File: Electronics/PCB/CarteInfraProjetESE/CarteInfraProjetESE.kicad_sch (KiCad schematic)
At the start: 4 parts

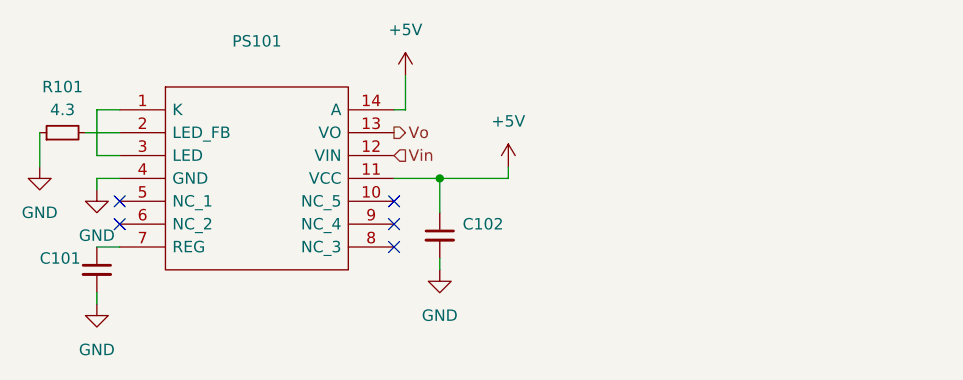
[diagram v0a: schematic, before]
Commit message: added test pin
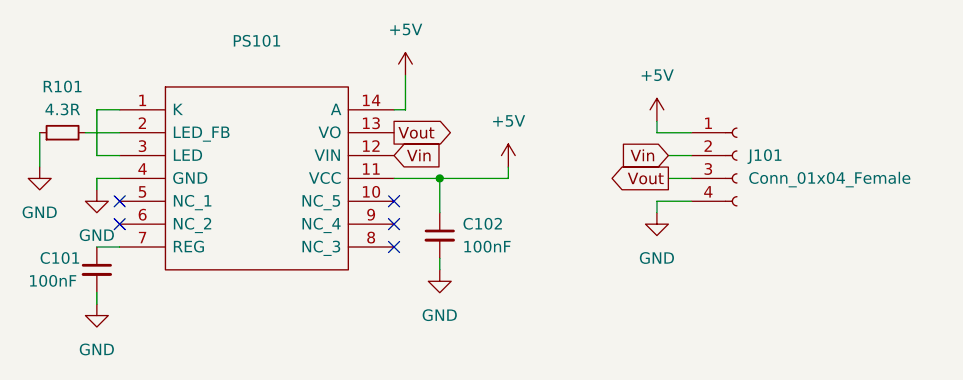
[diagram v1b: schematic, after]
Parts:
- added J101: Conn_01x04_Female, symbol Connector:Conn_01x04_Female
- C101, C102: value ~ -> 100nF
- R101: value 4.3 -> 4.3R
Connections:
- net +5V: now also J101.1 (Pin_1)
- net GND: now also J101.4 (Pin_4)
- net Vin: now also J101.2 (Pin_2)
- net Vo renamed Vout
- net Vout: now also J101.3 (Pin_3)
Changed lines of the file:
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@@
+    (stroke (width 0) (type default) (color 0 0 0 0))
+  )
+  (wire (pts (xy 191.77 74.93) (xy 194.31 74.93))
+    (stroke (width 0) (type default) (color 0 0 0 0))
+  )
+  (wire (pts (xy 190.5 71.12) (xy 190.5 72.39))
     (stroke (width 0) (type default) (color 0 0 0 0))
   )
@@
     (stroke (width 0) (type default) (color 0 0 0 0))
   )
+  (wire (pts (xy 190.5 72.39) (xy 194.31 72.39))
+    (stroke (width 0) (type default) (color 0 0 0 0))
+  )
   (wire (pts (xy 128.27 69.85) (xy 128.27 74.93))
     (stroke (width 0) (type default) (color 0 0 0 0))
   )
+  (wire (pts (xy 194.31 80.01) (xy 190.5 80.01))
+    (stroke (width 0) (type default) (color 0 0 0 0))
+  )
   (wire (pts (xy 166.37 87.63) (xy 166.37 86.36))
     (stroke (width 0) (type default) (color 0 0 0 0))
@@
     (stroke (width 0) (type default) (color 0 0 0 0))
   )
+  (wire (pts (xy 191.77 77.47) (xy 194.31 77.47))
+    (stroke (width 0) (type default) (color 0 0 0 0))
+  )
   (wire (pts (xy 128.27 91.44) (xy 128.27 90.17))
     (stroke (width 0) (type default) (color 0 0 0 0))
@@
     (stroke (width 0) (type default) (color 0 0 0 0))
   )
+  (wire (pts (xy 190.5 80.01) (xy 190.5 81.28))
+    (stroke (width 0) (type default) (color 0 0 0 0))
+  )
   (wire (pts (xy 130.81 77.47) (xy 128.27 77.47))
     (stroke (width 0) (type default) (color 0 0 0 0))
@@
     (stroke (width 0) (type default) (color 0 0 0 0))
   )
-  (hierarchical_label "Vo" (shape output) (at 161.29 72.39 0)
+  (global_label "Vin" (shape input) (at 191.77 74.93 180) (fields_autoplaced)
+    (effects (font (size 1.27 1.27)) (justify right))
+    (property "Intersheet References" "${INTERSHEET_REFS}" (id 0) (at 186.5145 75.0094 0)
+      (effects (font (size 1.27 1.27)) (justify right) hide)
+    )
+  )
+  (global_label "Vout" (shape output) (at 161.29 72.39 0) (fields_autoplaced)
     (effects (font (size 1.27 1.27)) (justify left))
-  )
-  (hierarchical_label "Vin" (shape input) (at 161.29 74.93 0)
+    (property "Intersheet References" "${INTERSHEET_REFS}" (id 0) (at 167.8155 72.3106 0)
+      (effects (font (size 1.27 1.27)) (justify left) hide)
+    )
+  )
+  (global_label "Vin" (shape input) (at 161.29 74.93 0) (fields_autoplaced)
     (effects (font (size 1.27 1.27)) (justify left))
+    (property "Intersheet References" "${INTERSHEET_REFS}" (id 0) (at 166.5455 74.8506 0)
+      (effects (font (size 1.27 1.27)) (justify left) hide)
+    )
+  )
+  (global_label "Vout" (shape output) (at 191.77 77.47 180) (fields_autoplaced)
+    (effects (font (size 1.27 1.27)) (justify right))
+    (property "Intersheet References" "${INTERSHEET_REFS}" (id 0) (at 185.2445 77.5494 0)
+      (effects (font (size 1.27 1.27)) (justify right) hide)
+    )
   )
   (symbol (lib_id "Device:C_Small") (at 128.27 87.63 0) (unit 1)
@@
       (effects (font (size 1.27 1.27)) (justify left))
     )
-    (property "Value" "~" (id 1) (at 120.65 88.9 0)
+    (property "Value" "100nF" (id 1) (at 120.65 88.9 0)
       (effects (font (size 1.27 1.27)) (justify left))
     )
@@
       (effects (font (size 1.27 1.27)) (justify left))
     )
-    (property "Value" "~" (id 1) (at 168.91 85.0962 0)
+    (property "Value" "100nF" (id 1) (at 168.91 85.0962 0)
       (effects (font (size 1.27 1.27)) (justify left))
     )
@@
     (pin "1")
   )
+  (symbol (lib_id "Connector:Conn_01x04_Female") (at 199.39 74.93 0) (unit 1)
+    (in_bom yes) (on_board yes) (fields_autoplaced)
+    (property "Reference" "J101" (id 0) (at 200.66 74.9299 0)
+      (effects (font (size 1.27 1.27)) (justify left))
+    )
+    (property "Value" "Conn_01x04_Female" (id 1) (at 200.66 77.4699 0)
+      (effects (font (size 1.27 1.27)) (justify left))
+    )
+    (property "Footprint" "" (id 2) (at 199.39 74.93 0)
+      (effects (font (size 1.27 1.27)) hide)
+    )
+    (property "Datasheet" "~" (id 3) (at 199.39 74.93 0)
+      (effects (font (size 1.27 1.27)) hide)
+    )
+    (pin "1")
+    (pin "2")
+    (pin "3")
+    (pin "4")
+  )
   (symbol (lib_id "power:+5V") (at 162.56 66.04 0) (unit 1)
     (in_bom yes) (on_board yes) (fields_autoplaced)
@@
     )
     (property "Datasheet" "" (id 3) (at 162.56 66.04 0)
+      (effects (font (size 1.27 1.27)) hide)
+    )
+    (pin "1")
+  )
+  (symbol (lib_id "power:GND") (at 190.5 81.28 0) (unit 1)
+    (in_bom yes) (on_board yes) (fields_autoplaced)
+    (property "Reference" "#PWR0107" (id 0) (at 190.5 87.63 0)
+      (effects (font (size 1.27 1.27)) hide)
+    )
+    (property "Value" "GND" (id 1) (at 190.5 86.36 0))
+    (property "Footprint" "" (id 2) (at 190.5 81.28 0)
+      (effects (font (size 1.27 1.27)) hide)
+    )
+    (property "Datasheet" "" (id 3) (at 190.5 81.28 0)
       (effects (font (size 1.27 1.27)) hide)
     )
@@
     (pin "1")
   )
+  (symbol (lib_id "power:+5V") (at 190.5 71.12 0) (unit 1)
+    (in_bom yes) (on_board yes) (fields_autoplaced)
+    (property "Reference" "#PWR0108" (id 0) (at 190.5 74.93 0)
+      (effects (font (size 1.27 1.27)) hide)
+    )
+    (property "Value" "+5V" (id 1) (at 190.5 66.04 0))
+    (property "Footprint" "" (id 2) (at 190.5 71.12 0)
+      (effects (font (size 1.27 1.27)) hide)
+    )
+    (property "Datasheet" "" (id 3) (at 190.5 71.12 0)
+      (effects (font (size 1.27 1.27)) hide)
+    )
+    (pin "1")
+  )
   (symbol (lib_id "Device:R_Small") (at 124.46 72.39 90) (unit 1)
     (in_bom yes) (on_board yes)
     (property "Reference" "R101" (id 0) (at 124.46 67.31 90))
-    (property "Value" "4.3" (id 1) (at 124.46 69.85 90))
+    (property "Value" "4.3R" (id 1) (at 124.46 69.85 90))
     (property "Footprint" "" (id 2) (at 124.46 72.39 0)
       (effects (font (size 1.27 1.27)) hide)
@@
       (reference "#PWR0106") (unit 1) (value "+5V") (footprint "")
     )
+    (path "/8538e3c5-8f61-4d4d-a072-64ef7b3c17d6"
+      (reference "#PWR0107") (unit 1) (value "GND") (footprint "")
+    )
+    (path "/e819225a-4d26-4021-97e7-923d871797c8"
+      (reference "#PWR0108") (unit 1) (value "+5V") (footprint "")
+    )
     (path "/3bb446a9-5ef3-46a9-8480-e76bab253a97"
-      (reference "C101") (unit 1) (value "~") (footprint "")
+      (reference "C101") (unit 1) (value "100nF") (footprint "")
     )
     (path "/40e43f3b-2ed3-409c-9d69-e53f9ad30810"
-      (reference "C102") (unit 1) (value "~") (footprint "")
+      (reference "C102") (unit 1) (value "100nF") (footprint "")
+    )
+    (path "/684f9b05-252d-4cae-824e-b33eec2296cd"
+      (reference "J101") (unit 1) (value "Conn_01x04_Female") (footprint "")
     )
     (path "/a3018cb8-4813-45e0-ae1b-04b6a2654dc6"
@@
     )
     (path "/e9e3e85d-0102-4b24-bb84-42fd6b5e1c3c"
-      (reference "R101") (unit 1) (value "4.3") (footprint "")
-    )
-  )
+      (reference "R101") (unit 1) (value "4.3R") (footprint "")
+    )
+  )
